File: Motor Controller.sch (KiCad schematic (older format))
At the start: 14 parts

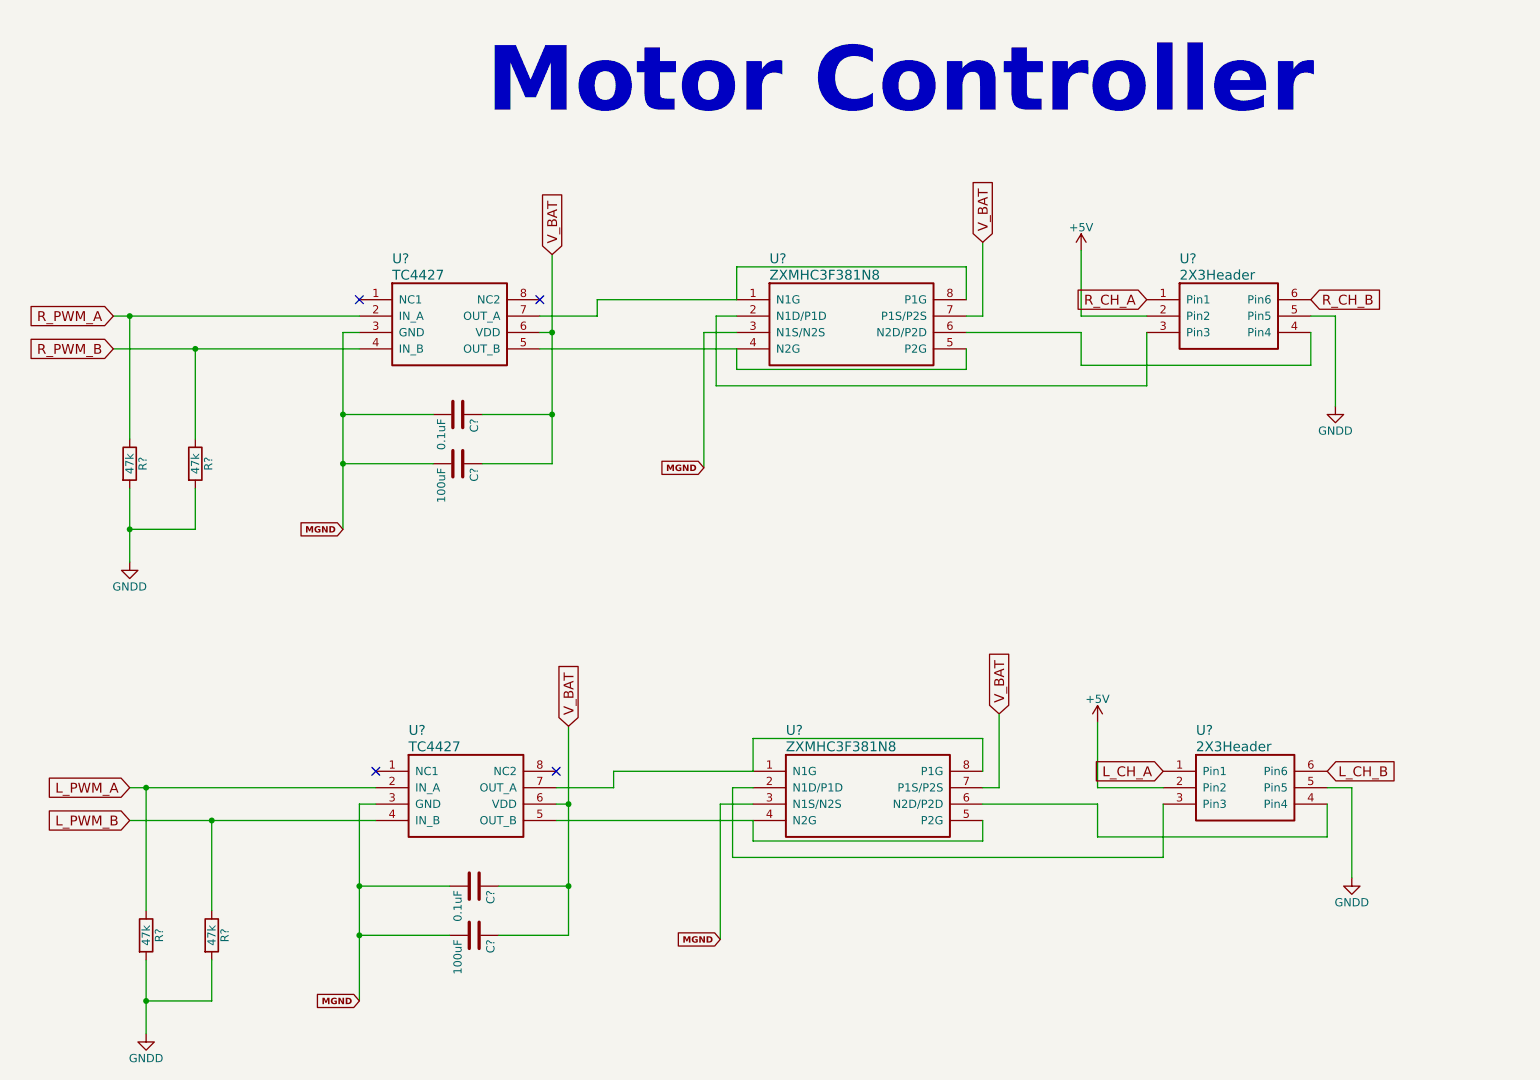
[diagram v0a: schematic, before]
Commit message: Created footprint for DC DC converter
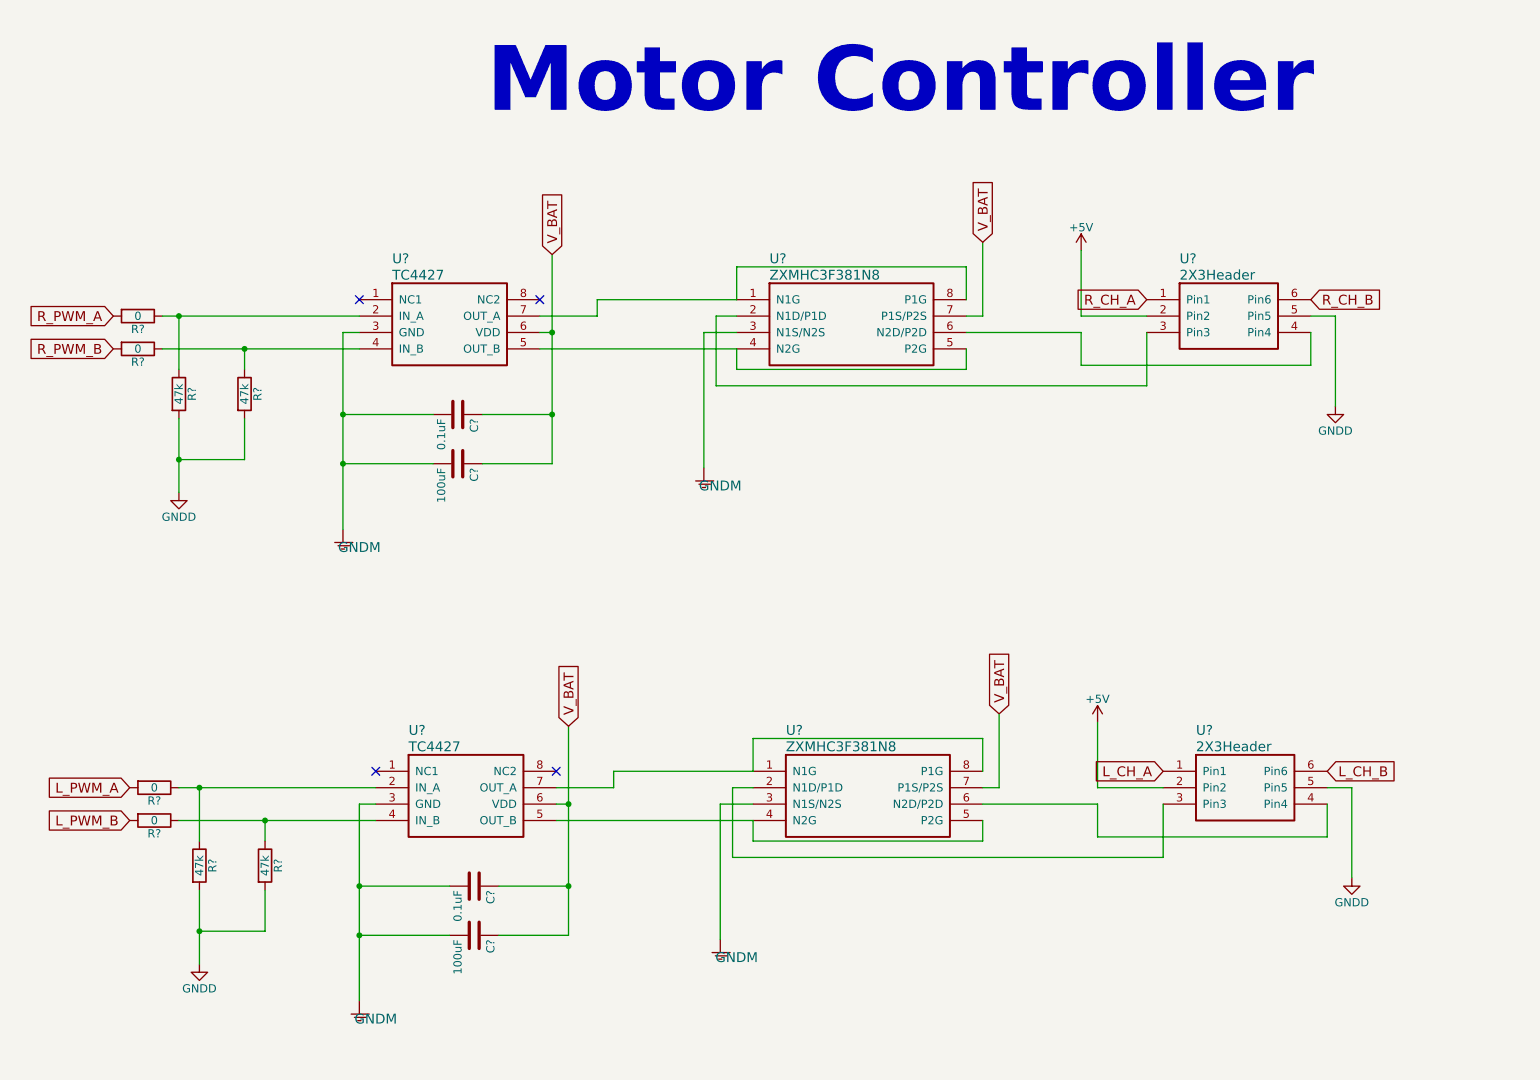
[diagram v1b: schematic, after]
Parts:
- added R? (x4): 0, symbol R
- added U? (x4): GNDM, symbol GNDM
- U? (x2): footprint (none) -> Housings_SOIC:Diodes_PSOP-8
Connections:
- net L_PWM_A: now also R?.2; no longer R?.1, U?.2 (IN_A)
- net L_PWM_B: now also R?.2; no longer R?.1, U?.4 (IN_B)
- net R_PWM_A: now also R?.2; no longer R?.1, U?.2 (IN_A)
- net R_PWM_B: now also R?.2; no longer R?.1, U?.4 (IN_B)
- removed net MGND: C?.2, C?.2, C?.2, C?.2, U?.3 (GND), U?.3 (GND), U?.3 (N1S/N2S), U?.3 (N1S/N2S)
- new net: R?.1, R?.1, U?.2 (IN_A) (x2)
- new net: C?.2, C?.2, U?.1, U?.3 (GND) (x2)
- new net: R?.1, R?.1, U?.4 (IN_B) (x2)
- new net: U?.1, U?.3 (N1S/N2S) (x2)
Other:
- moved on the sheet: R?

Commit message: created footprint for linear requlator
added footprint for microcontroller linear requlator
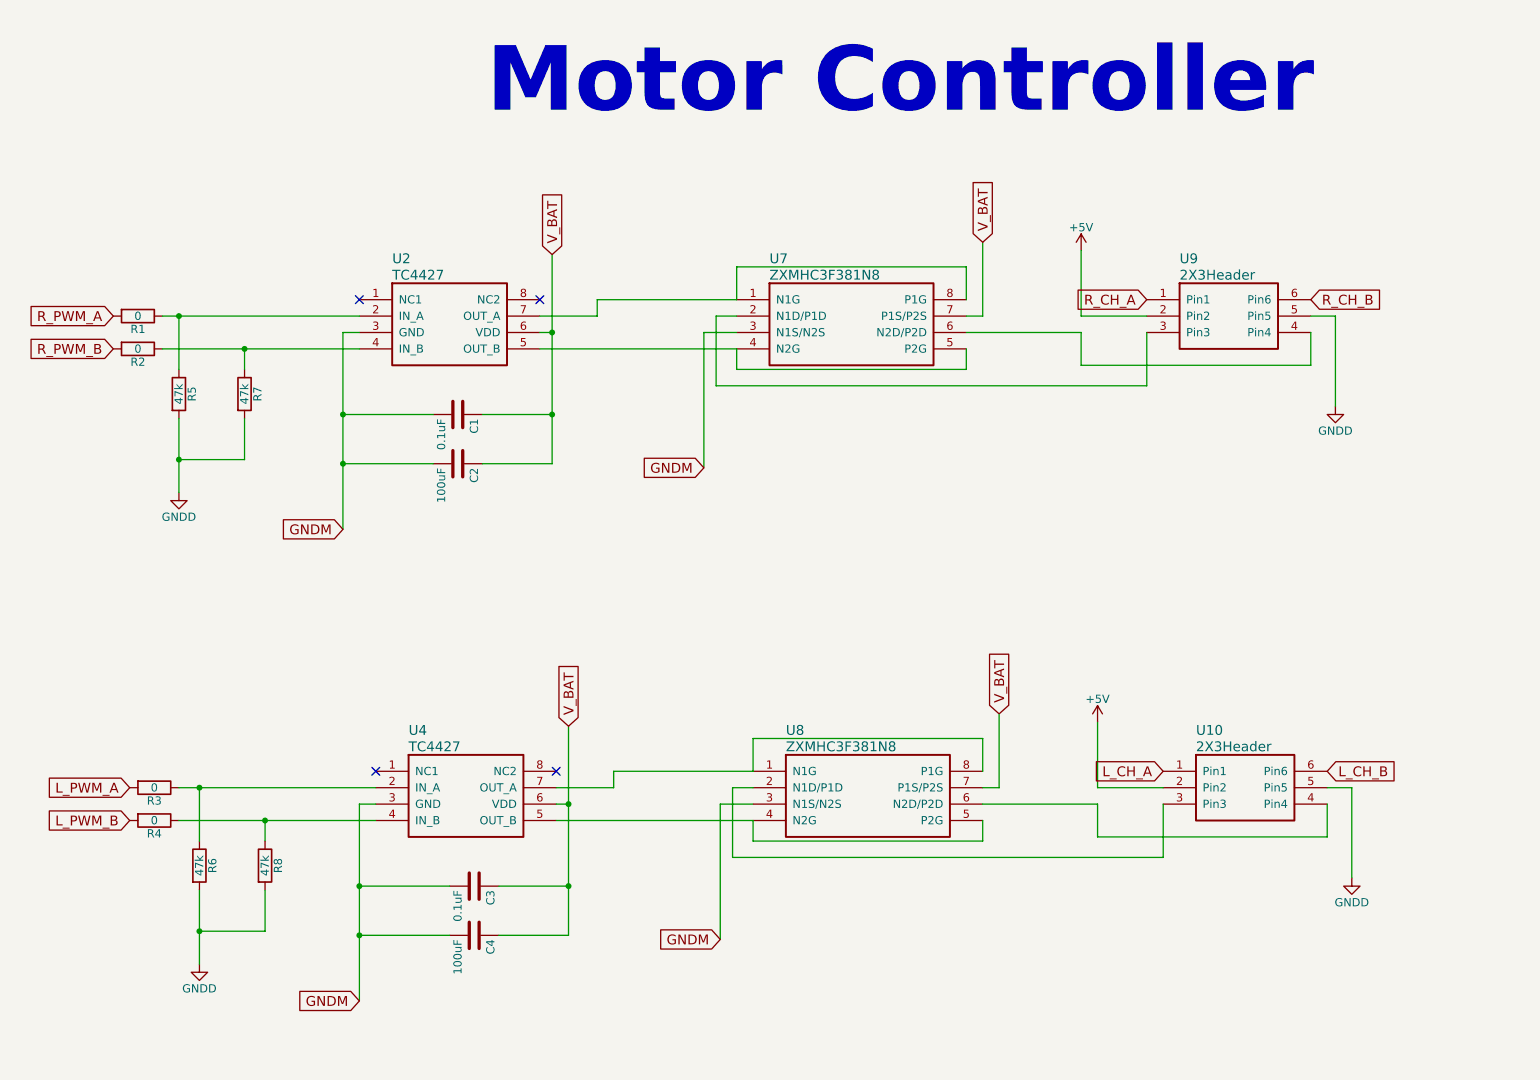
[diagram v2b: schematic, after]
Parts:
- removed U? (x4): GNDM, symbol GNDM
- C1, C2, C3, C4: renamed from C?; footprint (none) -> Capacitors_SMD:C_0603
- R1, R2, R3, R4, R5, R6, R7, R8: renamed from R?; footprint (none) -> Resistors_SMD:R_0603
- U10, U9: renamed from U?; footprint (none) -> Socket_Strips:Socket_Strip_Straight_2x03_Pitch2.54mm
- U2, U4: renamed from U?; footprint (none) -> sop:MSOP8
- gave numbers to parts that had none: 2
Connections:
- net GNDM: now reaches C1.2, C2.2, U2.3 (GND)
- net GNDM: now also C3.2, C4.2, U4.3 (GND), U7.3 (N1S/N2S), U8.3 (N1S/N2S)
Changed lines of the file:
@@
 $EndDescr
 $Comp
-L TC4427 U?
+L TC4427 U2
 U 1 1 5945E3C6
 P 2500 2200
-F 0 "U?" H 2700 2450 60  0000 L CNN
+F 0 "U2" H 2700 2450 60  0000 L CNN
 F 1 "TC4427" H 2700 2350 60  0000 L CNN
-F 2 "" H 2500 2200 60  0001 C CNN
+F 2 "sop:MSOP8" H 2500 2200 60  0001 C CNN
 F 3 "" H 2500 2200 60  0001 C CNN
 	1    2500 2200
@@
 $EndComp
 $Comp
-L ZXMHC3F381N8 U?
+L ZXMHC3F381N8 U7
 U 1 1 5945E3EF
 P 4800 2200
-F 0 "U?" H 5000 2450 60  0000 L CNN
+F 0 "U7" H 5000 2450 60  0000 L CNN
 F 1 "ZXMHC3F381N8" H 5000 2350 60  0000 L CNN
 F 2 "Housings_SOIC:Diodes_PSOP-8" H 4800 2200 60  0001 C CNN
@@
 $EndComp
 $Comp
-L 2X3Header U?
+L 2X3Header U9
 U 1 1 5945E464
 P 7300 2200
-F 0 "U?" H 7500 2450 60  0000 L CNN
+F 0 "U9" H 7500 2450 60  0000 L CNN
 F 1 "2X3Header" H 7500 2350 60  0000 L CNN
-F 2 "" H 7300 2200 60  0001 C CNN
+F 2 "Socket_Strips:Socket_Strip_Straight_2x03_Pitch2.54mm" H 7300 2200 60  0001 C CNN
 F 3 "" H 7300 2200 60  0001 C CNN
 	1    7300 2200
@@
 $EndComp
 $Comp
-L R R?
+L R R5
 U 1 1 5945E536
 P 1400 2775
-F 0 "R?" V 1480 2775 50  0000 C CNN
+F 0 "R5" V 1480 2775 50  0000 C CNN
 F 1 "47k" V 1400 2775 50  0000 C CNN
-F 2 "" V 1330 2775 50  0001 C CNN
+F 2 "Resistors_SMD:R_0603" V 1330 2775 50  0001 C CNN
 F 3 "" H 1400 2775 50  0001 C CNN
 	1    1400 2775
@@
 $EndComp
 $Comp
-L R R?
+L R R7
 U 1 1 5945E56D
 P 1800 2775
-F 0 "R?" V 1880 2775 50  0000 C CNN
+F 0 "R7" V 1880 2775 50  0000 C CNN
 F 1 "47k" V 1800 2775 50  0000 C CNN
-F 2 "" V 1730 2775 50  0001 C CNN
+F 2 "Resistors_SMD:R_0603" V 1730 2775 50  0001 C CNN
 F 3 "" H 1800 2775 50  0001 C CNN
 	1    1800 2775
@@
 $EndComp
 $Comp
-L C C?
+L C C1
 U 1 1 5945E595
 P 3100 2900
-F 0 "C?" H 3125 3000 50  0000 L CNN
+F 0 "C1" H 3125 3000 50  0000 L CNN
 F 1 "0.1uF" H 3125 2800 50  0000 L CNN
-F 2 "" H 3138 2750 50  0001 C CNN
+F 2 "Capacitors_SMD:C_0603" H 3138 2750 50  0001 C CNN
 F 3 "" H 3100 2900 50  0001 C CNN
 	1    3100 2900
@@
 $EndComp
 $Comp
-L C C?
+L C C2
 U 1 1 5945E5DD
 P 3100 3200
-F 0 "C?" H 3125 3300 50  0000 L CNN
+F 0 "C2" H 3125 3300 50  0000 L CNN
 F 1 "100uF" H 3125 3100 50  0000 L CNN
-F 2 "" H 3138 3050 50  0001 C CNN
+F 2 "Capacitors_SMD:C_0603" H 3138 3050 50  0001 C CNN
 F 3 "" H 3100 3200 50  0001 C CNN
 	1    3100 3200
@@
 $EndComp
 $Comp
-L GNDD #PWR?
+L GNDD #PWR01
 U 1 1 5945E5FF
 P 1400 3375
-F 0 "#PWR?" H 1400 3125 50  0001 C CNN
+F 0 "#PWR01" H 1400 3125 50  0001 C CNN
 F 1 "GNDD" H 1400 3225 50  0000 C CNN
 F 2 "" H 1400 3375 50  0001 C CNN
@@
 R_CH_B
 $Comp
-L GNDD #PWR?
+L GNDD #PWR02
 U 1 1 5945ED1F
 P 8450 2850
-F 0 "#PWR?" H 8450 2600 50  0001 C CNN
+F 0 "#PWR02" H 8450 2600 50  0001 C CNN
 F 1 "GNDD" H 8450 2700 50  0000 C CNN
 F 2 "" H 8450 2850 50  0001 C CNN
@@
 $EndComp
 $Comp
-L +5V #PWR?
+L +5V #PWR03
 U 1 1 5945ED79
 P 6900 1900
-F 0 "#PWR?" H 6900 1750 50  0001 C CNN
+F 0 "#PWR03" H 6900 1750 50  0001 C CNN
 F 1 "+5V" H 6900 2040 50  0000 C CNN
 F 2 "" H 6900 1900 50  0001 C CNN
@@
 V_BAT
 $Comp
-L TC4427 U?
+L TC4427 U4
 U 1 1 5945EF70
 P 2600 5075
-F 0 "U?" H 2800 5325 60  0000 L CNN
+F 0 "U4" H 2800 5325 60  0000 L CNN
 F 1 "TC4427" H 2800 5225 60  0000 L CNN
-F 2 "" H 2600 5075 60  0001 C CNN
+F 2 "sop:MSOP8" H 2600 5075 60  0001 C CNN
 F 3 "" H 2600 5075 60  0001 C CNN
 	1    2600 5075
@@
 $EndComp
 $Comp
-L ZXMHC3F381N8 U?
+L ZXMHC3F381N8 U8
 U 1 1 5945EF76
 P 4900 5075
-F 0 "U?" H 5100 5325 60  0000 L CNN
+F 0 "U8" H 5100 5325 60  0000 L CNN
 F 1 "ZXMHC3F381N8" H 5100 5225 60  0000 L CNN
 F 2 "Housings_SOIC:Diodes_PSOP-8" H 4900 5075 60  0001 C CNN
@@
 $EndComp
 $Comp
-L 2X3Header U?
+L 2X3Header U10
 U 1 1 5945EF7C
 P 7400 5075
-F 0 "U?" H 7600 5325 60  0000 L CNN
+F 0 "U10" H 7600 5325 60  0000 L CNN
 F 1 "2X3Header" H 7600 5225 60  0000 L CNN
-F 2 "" H 7400 5075 60  0001 C CNN
+F 2 "Socket_Strips:Socket_Strip_Straight_2x03_Pitch2.54mm" H 7400 5075 60  0001 C CNN
 F 3 "" H 7400 5075 60  0001 C CNN
 	1    7400 5075
@@
 $EndComp
 $Comp
-L R R?
+L R R6
 U 1 1 5945EF82
 P 1525 5650
-F 0 "R?" V 1605 5650 50  0000 C CNN
+F 0 "R6" V 1605 5650 50  0000 C CNN
 F 1 "47k" V 1525 5650 50  0000 C CNN
-F 2 "" V 1455 5650 50  0001 C CNN
+F 2 "Resistors_SMD:R_0603" V 1455 5650 50  0001 C CNN
 F 3 "" H 1525 5650 50  0001 C CNN
 	1    1525 5650
@@
 $EndComp
 $Comp
-L R R?
+L R R8
 U 1 1 5945EF88
 P 1925 5650
-F 0 "R?" V 2005 5650 50  0000 C CNN
+F 0 "R8" V 2005 5650 50  0000 C CNN
 F 1 "47k" V 1925 5650 50  0000 C CNN
-F 2 "" V 1855 5650 50  0001 C CNN
+F 2 "Resistors_SMD:R_0603" V 1855 5650 50  0001 C CNN
 F 3 "" H 1925 5650 50  0001 C CNN
 	1    1925 5650
@@
 $EndComp
 $Comp
-L C C?
+L C C3
 U 1 1 5945EF8E
 P 3200 5775
-F 0 "C?" H 3225 5875 50  0000 L CNN
+F 0 "C3" H 3225 5875 50  0000 L CNN
 F 1 "0.1uF" H 3225 5675 50  0000 L CNN
-F 2 "" H 3238 5625 50  0001 C CNN
+F 2 "Capacitors_SMD:C_0603" H 3238 5625 50  0001 C CNN
 F 3 "" H 3200 5775 50  0001 C CNN
 	1    3200 5775
@@
 $EndComp
 $Comp
-L C C?
+L C C4
 U 1 1 5945EF94
 P 3200 6075
-F 0 "C?" H 3225 6175 50  0000 L CNN
+F 0 "C4" H 3225 6175 50  0000 L CNN
 F 1 "100uF" H 3225 5975 50  0000 L CNN
-F 2 "" H 3238 5925 50  0001 C CNN
+F 2 "Capacitors_SMD:C_0603" H 3238 5925 50  0001 C CNN
 F 3 "" H 3200 6075 50  0001 C CNN
 	1    3200 6075
@@
 $EndComp
 $Comp
-L GNDD #PWR?
+L GNDD #PWR04
 U 1 1 5945EF9A
 P 1525 6250
-F 0 "#PWR?" H 1525 6000 50  0001 C CNN
+F 0 "#PWR04" H 1525 6000 50  0001 C CNN
 F 1 "GNDD" H 1525 6100 50  0000 C CNN
 F 2 "" H 1525 6250 50  0001 C CNN
@@
 L_CH_B
 $Comp
-L GNDD #PWR?
+L GNDD #PWR05
 U 1 1 5945EFE1
 P 8550 5725
-F 0 "#PWR?" H 8550 5475 50  0001 C CNN
+F 0 "#PWR05" H 8550 5475 50  0001 C CNN
 F 1 "GNDD" H 8550 5575 50  0000 C CNN
 F 2 "" H 8550 5725 50  0001 C CNN
@@
 $EndComp
 $Comp
-L +5V #PWR?
+L +5V #PWR06
 U 1 1 5945EFE7
 P 7000 4775
-F 0 "#PWR?" H 7000 4625 50  0001 C CNN
+F 0 "#PWR06" H 7000 4625 50  0001 C CNN
 F 1 "+5V" H 7000 4915 50  0000 C CNN
 F 2 "" H 7000 4775 50  0001 C CNN
@@
 Motor Controller \n
 $Comp
-L GNDM U?
-U 1 1 594B755F
-P 2400 3700
-F 0 "U?" H 2500 3610 60  0001 C CNN
-F 1 "GNDM" H 2500 3690 60  0000 C CNN
-F 2 "" H 2400 3700 60  0001 C CNN
-F 3 "" H 2400 3700 60  0001 C CNN
-	1    2400 3700
-	1    0    0    -1
-$EndComp
-$Comp
-L GNDM U?
-U 1 1 594B7619
-P 4600 3325
-F 0 "U?" H 4700 3235 60  0001 C CNN
-F 1 "GNDM" H 4700 3315 60  0000 C CNN
-F 2 "" H 4600 3325 60  0001 C CNN
-F 3 "" H 4600 3325 60  0001 C CNN
-	1    4600 3325
-	1    0    0    -1
-$EndComp
-$Comp
-L GNDM U?
-U 1 1 594B77D5
-P 4700 6200
-F 0 "U?" H 4800 6110 60  0001 C CNN
-F 1 "GNDM" H 4800 6190 60  0000 C CNN
-F 2 "" H 4700 6200 60  0001 C CNN
-F 3 "" H 4700 6200 60  0001 C CNN
-	1    4700 6200
-	1    0    0    -1
-$EndComp
-$Comp
-L GNDM U?
-U 1 1 594B78C9
-P 2500 6575
-F 0 "U?" H 2600 6485 60  0001 C CNN
-F 1 "GNDM" H 2600 6565 60  0000 C CNN
-F 2 "" H 2500 6575 60  0001 C CNN
-F 3 "" H 2500 6575 60  0001 C CNN
-	1    2500 6575
-	1    0    0    -1
-$EndComp
-$Comp
-L R R?
+L R R2
 U 1 1 594B8BDB
 P 1150 2500
-F 0 "R?" V 1230 2500 50  0000 C CNN
+F 0 "R2" V 1230 2500 50  0000 C CNN
 F 1 "0" V 1150 2500 50  0000 C CNN
-F 2 "" V 1080 2500 50  0001 C CNN
+F 2 "Resistors_SMD:R_0603" V 1080 2500 50  0001 C CNN
 F 3 "" H 1150 2500 50  0001 C CNN
 	1    1150 2500
@@
 $EndComp
 $Comp
-L R R?
+L R R1
 U 1 1 594B8CA5
 P 1150 2300
-F 0 "R?" V 1230 2300 50  0000 C CNN
+F 0 "R1" V 1230 2300 50  0000 C CNN
 F 1 "0" V 1150 2300 50  0000 C CNN
-F 2 "" V 1080 2300 50  0001 C CNN
+F 2 "Resistors_SMD:R_0603" V 1080 2300 50  0001 C CNN
 F 3 "" H 1150 2300 50  0001 C CNN
 	1    1150 2300
@@
 Connection ~ 1800 2500
 $Comp
-L R R?
+L R R3
 U 1 1 594B96FA
 P 1250 5175
-F 0 "R?" V 1330 5175 50  0000 C CNN
+F 0 "R3" V 1330 5175 50  0000 C CNN
 F 1 "0" V 1250 5175 50  0000 C CNN
-F 2 "" V 1180 5175 50  0001 C CNN
+F 2 "Resistors_SMD:R_0603" V 1180 5175 50  0001 C CNN
 F 3 "" H 1250 5175 50  0001 C CNN
 	1    1250 5175
@@
 $EndComp
 $Comp
-L R R?
+L R R4
 U 1 1 594B9756
 P 1250 5375
-F 0 "R?" V 1330 5375 50  0000 C CNN
+F 0 "R4" V 1330 5375 50  0000 C CNN
 F 1 "0" V 1250 5375 50  0000 C CNN
-F 2 "" V 1180 5375 50  0001 C CNN
+F 2 "Resistors_SMD:R_0603" V 1180 5375 50  0001 C CNN
 F 3 "" H 1250 5375 50  0001 C CNN
 	1    1250 5375
@@
 EndData
 $EndBitmap
+Text GLabel 4600 3225 0    60   Input ~ 0
+GNDM
+Text GLabel 2400 3600 0    60   Input ~ 0
+GNDM
+Text GLabel 2500 6475 0    60   Input ~ 0
+GNDM
+Text GLabel 4700 6100 0    60   Input ~ 0
+GNDM
 $EndSCHEMATC
